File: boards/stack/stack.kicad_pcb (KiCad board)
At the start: 2 copper layers, 100 x 100 mm, 79 parts, among them J1 SSW-120-02-G-D-RA, J2 61304021021, J3 SSW-120-02-G-D-RA, J4 SSW-120-02-G-D-RA, U1 74HC139, U10 74HC244, U11 74HC74, U12 74HC32, U13 74HC32, U14 74HC00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

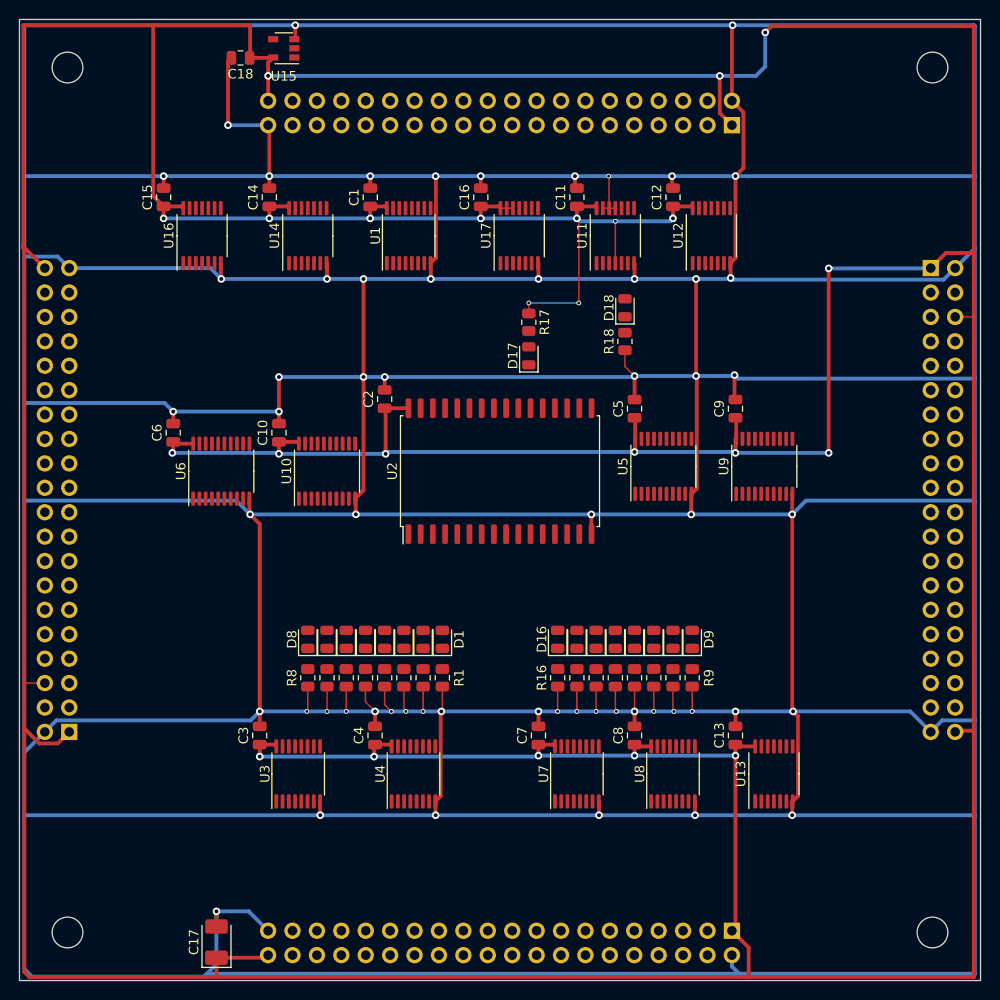
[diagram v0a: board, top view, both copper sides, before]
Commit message: Stack: power nets
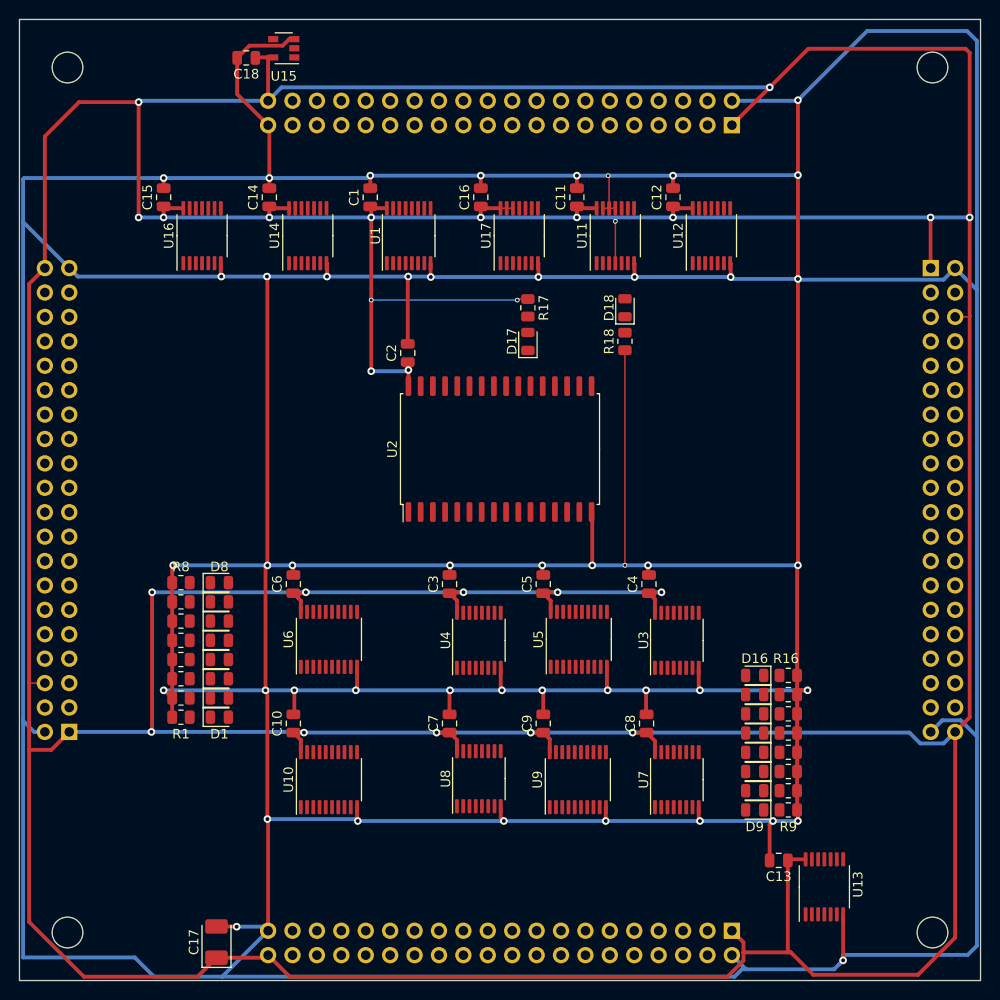
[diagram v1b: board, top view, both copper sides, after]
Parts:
- moved U3 41.8 mm to (118.4, 114.6)
- moved C9 38.4 mm to (104.5, 123.2)
- moved U9 37.9 mm to (108.1, 129.1)
- moved C4 32.6 mm to (115.5, 108.8)
- moved U10 32.1 mm to (82.2, 129.1)
- moved C10 30.3 mm to (78.5, 123.2)
- moved R1 27.5 mm to (66.8, 122.6), turned to 0 degrees
- moved R2 25.3 mm to (66.8, 120.6), turned to 0 degrees
- moved C3 25.3 mm to (94.8, 108.8)
- moved D1 24.6 mm to (70.8, 122.6), turned to 0 degrees
- moved R16 24.0 mm to (130.0, 118.2), turned to 180 degrees
- moved R3 23.2 mm to (66.8, 118.6), turned to 0 degrees
- moved R15 22.1 mm to (130.0, 120.2), turned to 180 degrees
- moved D2 22.1 mm to (70.8, 120.6), turned to 0 degrees
- moved R4 21.3 mm to (66.8, 116.6), turned to 0 degrees
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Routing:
- net GND: track 1278.4 -> 977.5 mm, vias 59 -> 47
- net VCC: track 763.5 -> 772.5 mm, vias 24 -> 26

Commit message: Stack: board
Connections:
- U5 pad 11: /Stack Pointer 0/c7 -> /Stack Pointer 0/c1
- U5 pad 13: /Stack Pointer 0/c6 -> /Stack Pointer 0/c0
- U5 pad 16: /d1 -> /d7
- U5 pad 18: /d0 -> /d6
- U5 pad 2: /Stack Pointer 0/c0 -> /Stack Pointer 0/c6
- U5 pad 4: /Stack Pointer 0/c1 -> /Stack Pointer 0/c7
- U5 pad 7: /d6 -> /d0
- U5 pad 9: /d7 -> /d1
- U9 pad 11: /Stack Pointer 1/c7 -> /Stack Pointer 1/c1
- U9 pad 13: /Stack Pointer 1/c6 -> /Stack Pointer 1/c0
- U9 pad 16: /d1 -> /d7
- U9 pad 18: /d0 -> /d6
- U9 pad 2: /Stack Pointer 1/c0 -> /Stack Pointer 1/c6
- U9 pad 4: /Stack Pointer 1/c1 -> /Stack Pointer 1/c7
- U9 pad 7: /d6 -> /d0
- U9 pad 9: /d7 -> /d1
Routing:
- net /a1: track 0.00 -> 282.2 mm, vias 0 -> 10
- net /a0: track 0.00 -> 269.9 mm, vias 0 -> 9
- net /d1: track 0.00 -> 268.5 mm, vias 0 -> 17
- net /~rst: track 0.00 -> 266.9 mm, vias 0 -> 13
- net /a15: track 0.00 -> 266.1 mm, vias 0 -> 7
- net /d3: track 0.00 -> 265.5 mm, vias 0 -> 15
- net /~we: track 0.00 -> 263.3 mm, vias 0 -> 18
- net /d2: track 0.00 -> 260.3 mm, vias 0 -> 17
- net /a14: track 0.00 -> 259.6 mm, vias 0 -> 7
- net /d0: track 0.00 -> 256.9 mm, vias 0 -> 19
- net /rdy: track 0.00 -> 254.3 mm, vias 0 -> 3
- net GND: track 977.5 -> 1226.8 mm, vias 47 -> 62
- net /a9: track 0.00 -> 248.8 mm, vias 0 -> 9
- net /~oe: track 0.00 -> 243.9 mm, vias 0 -> 9
- net /a3: track 0.00 -> 241.3 mm, vias 0 -> 7
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- added copper zone on B.Cu, net GND
- added copper zone on F.Cu, net VCC
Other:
- board text added: "0"
- board text added: "7"
- board text added: "Licensed under the TAPR OHL www.tapr.org/OHL"
- board text added: "SP0"
- board text added: "SP1"
- board text added: "Stack rev.1"
- board text added: "access"
- board text added: "enable"
